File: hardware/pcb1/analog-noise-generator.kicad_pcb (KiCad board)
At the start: 4 copper layers, 12.7 x 45.6 mm, 90 parts, among them J1 USB_C_Receptacle_USB2.0, J2 Conn_01x03_Pin, J5 Conn_01x04_Pin, J6 Conn_01x04_Pin, J7 Conn_01x02_Pin, J9 Conn_02x04_Odd_Even, U1 STM32F072CBTx, U2 USBLC6-2SC6, U3 LR8321A-T33, U4 LIS2DH12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

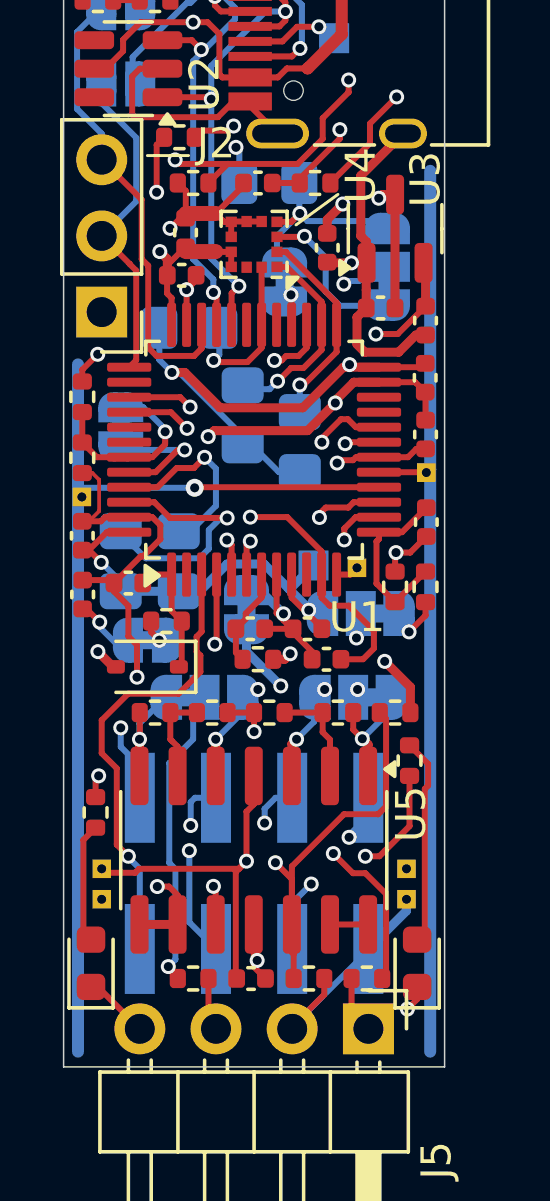
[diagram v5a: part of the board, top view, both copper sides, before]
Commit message: fix some issues for JLC
- increase some clearances that were marked as "danger" in their DFM
- change value of C12, so it won't be grouped with the incompatible 100 nF caps
- add image to README
- rotate U2 in CPL file
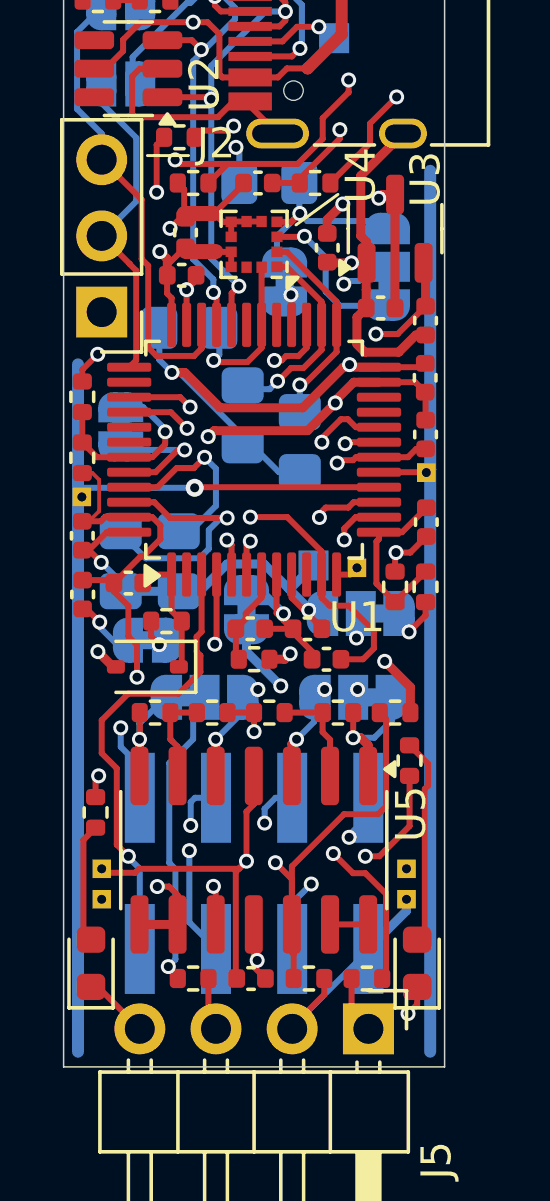
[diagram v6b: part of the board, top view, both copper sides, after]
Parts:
- C12: value 100n, 50V -> 100n_50V
- moved R8 0.13 mm to (111.8, 88.5)
- moved NT1 0.05 mm to (109.9, 73.7)
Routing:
- net Net-(JP4-A): track 4.11 -> 4.76 mm
